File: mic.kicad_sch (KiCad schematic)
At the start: 0 parts

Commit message: added ADAU7002 Symbol
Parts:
- added U3: ~, symbol mic_patch_parts:AUD_00001
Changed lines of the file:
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@@
 	(generator_version "8.0")
 	(paper "A4")
+	(symbol
+		(lib_id "mic_patch_parts:AUD_00001")
+		(at 59.69 43.18 0)
+		(unit 1)
+		(exclude_from_sim no)
+		(in_bom yes)
+		(on_board yes)
+		(dnp no)
+		(fields_autoplaced yes)
+		(property "Reference" "U3"
+			(at 59.69 27.94 0)
+			(effects
+				(font
+					(size 1.27 1.27)
+				)
+			)
+		)
+		(property "Value" "~"
+			(at 59.69 29.21 0)
+			(effects
+				(font
+					(size 1.27 1.27)
+				)
+			)
+		)
+		(property "Footprint" ""
+			(at 66.294 51.308 0)
+			(effects
+				(font
+					(size 1.27 1.27)
+				)
+				(hide yes)
+			)
+		)
+		(property "Datasheet" "https://www.lcsc.com/datasheet/lcsc_datasheet_2001132235_Analog-Devices-ADAU7002ACBZ-R7_C481886.pdf"
+			(at 65.024 59.69 0)
+			(effects
+				(font
+					(size 1.27 1.27)
+				)
+				(hide yes)
+			)
+		)
+		(property "Description" ""
+			(at 62.484 32.004 0)
+			(effects
+				(font
+					(size 1.27 1.27)
+				)
+				(hide yes)
+			)
+		)
+		(property "Desc" "ADAU7002 I2S to PDM Converter"
+			(at 59.69 31.75 0)
+			(effects
+				(font
+					(size 1.27 1.27)
+				)
+			)
+		)
+		(property "LCSC PNs" "C481886"
+			(at 67.31 53.594 0)
+			(effects
+				(font
+					(size 1.27 1.27)
+				)
+				(hide yes)
+			)
+		)
+		(property "MPNs" "ADAU7002ACBZ-R7"
+			(at 59.69 34.29 0)
+			(effects
+				(font
+					(size 1.27 1.27)
+				)
+			)
+		)
+		(pin "B1"
+		)
+		(pin "A1"
+		)
+		(pin "A2"
+		)
+		(pin "B2"
+		)
+		(pin "C1"
+		)
+		(pin "C2"
+		)
+		(pin "D1"
+		)
+		(pin "D2"
+		)
+		(instances
+			(project "mic_patch_v1"
+				(path "/5448a297-4261-40a5-8009-47199bfe22cb/134a282e-9ca3-4100-8ce3-f798951ef007"
+					(reference "U3")
+					(unit 1)
+				)
+			)
+		)
+	)
 )

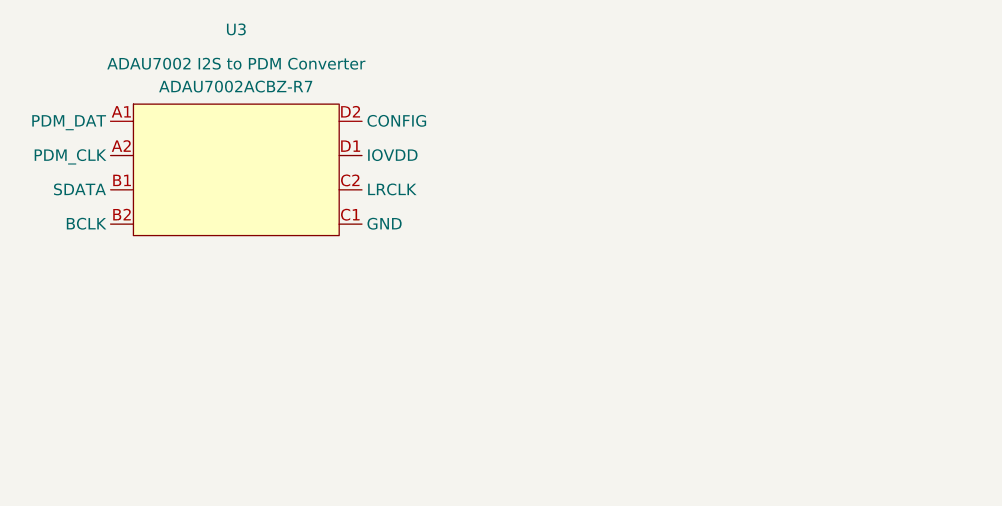
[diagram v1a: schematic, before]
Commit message: added MEMS microphone symbol
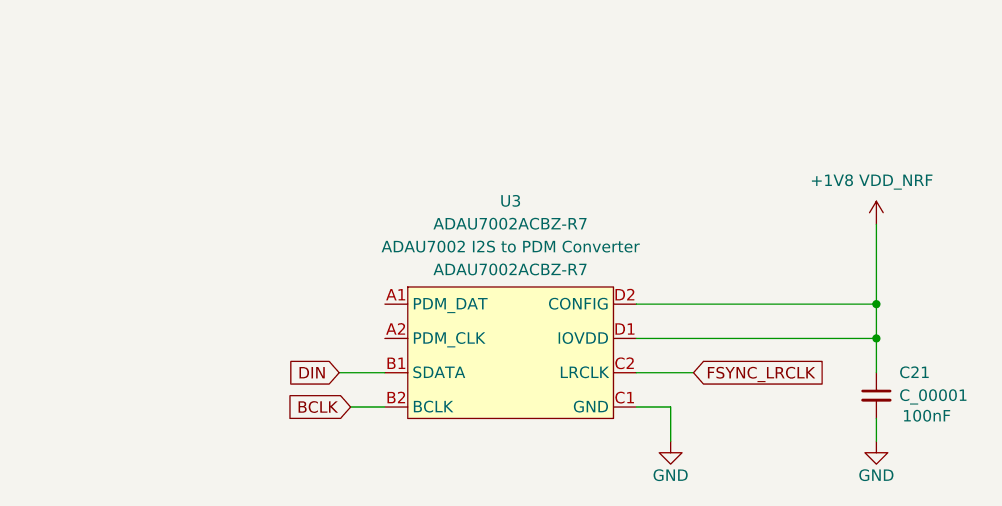
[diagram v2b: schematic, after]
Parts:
- added C21: C_00001, symbol mic_patch_parts:C_00001
- U3: value ~ -> ADAU7002ACBZ-R7
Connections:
- net DIN: now reaches U3.B1 (SDATA)
- net BCLK: now reaches U3.B2 (BCLK)
- net GND: now reaches U3.C1 (GND)
- net GND: now also C21.2
- net FSYNC_LRCLK: now reaches U3.C2 (LRCLK)
- net +1V8 VDD_NRF: now reaches U3.D1 (IOVDD)
- net +1V8 VDD_NRF: now also U3.D2 (CONFIG), C21.1

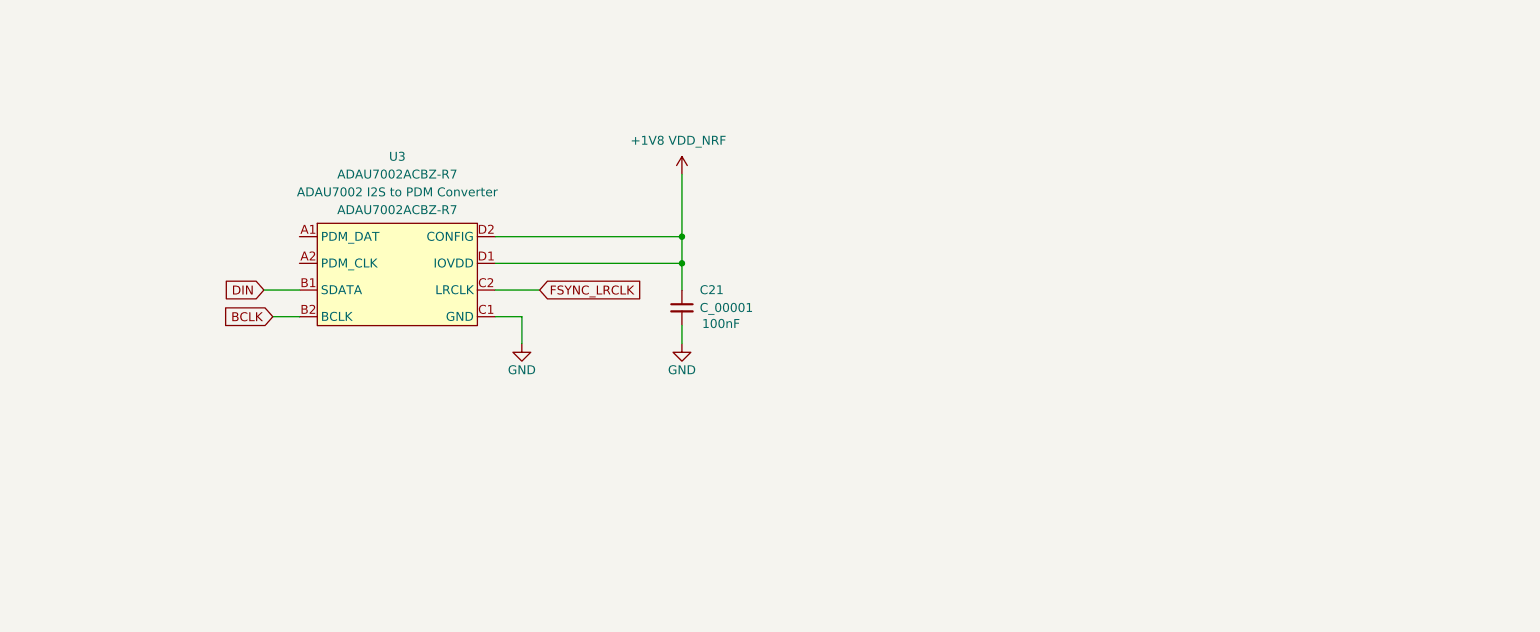
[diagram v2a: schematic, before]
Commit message: added rudimentary RF matching network
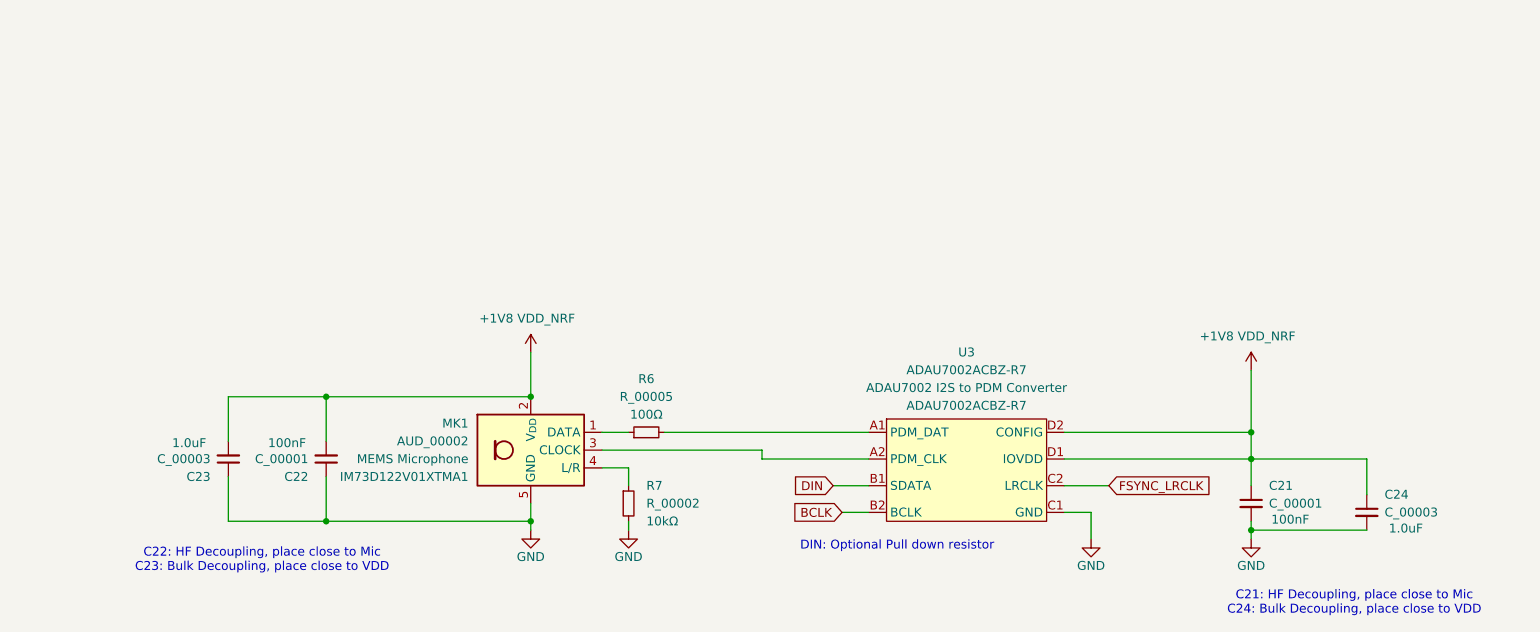
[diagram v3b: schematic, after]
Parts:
- added C22: C_00001, symbol mic_patch_parts:C_00001
- added C23, C24: C_00003, symbol mic_patch_parts:C_00003
- added MK1: AUD_00002, symbol mic_patch_parts:AUD_00002
- added R6: R_00005, symbol mic_patch_parts:R_00005
- added R7: R_00002, symbol mic_patch_parts:R_00003
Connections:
- net +1V8 VDD_NRF: now also C22.2, C23.2, C24.1, MK1.2 (V_{DD})
- net GND: now also C22.1, C23.1, C24.2, MK1.5 (GND), R7.2
- net at U3.A1 (PDM_DAT): now also R6.2
- net at U3.A2 (PDM_CLK): now also MK1.3 (CLOCK)
- new net: MK1.1 (DATA), R6.1
- new net: MK1.4 (L/R), R7.1
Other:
- note added: "C21: HF Decoupling, place close to Mic C24: Bulk Decoupling, place close to VDD"
- note added: "C22: HF Decoupling, place close to Mic C23: Bulk Decoupling, place close to VDD"
- note added: "DIN: Optional Pull down resistor"
- moved on the sheet: C21, U3

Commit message: updated power supply to 3.0V to support micro SD card
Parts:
- removed C24: C_00003, symbol mic_patch_parts:C_00003
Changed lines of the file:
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@@
-	)
-	(junction
-		(at 212.09 100.33)
-		(diameter 0)
-		(color 0 0 0 0)
 	)
 	(junction
@@
 	(wire
 		(pts
-			(xy 212.09 90.17) (xy 228.6 90.17)
-		)
-		(stroke
-			(width 0)
-			(type default)
-		)
-	)
-	(wire
-		(pts
-			(xy 212.09 99.06) (xy 212.09 100.33)
+			(xy 212.09 99.06) (xy 212.09 101.6)
 		)
 		(stroke
@@
 	(wire
 		(pts
-			(xy 212.09 100.33) (xy 228.6 100.33)
-		)
-		(stroke
-			(width 0)
-			(type default)
-		)
-	)
-	(wire
-		(pts
 			(xy 66.04 92.71) (xy 66.04 99.06)
 		)
@@
 		(pts
 			(xy 185.42 90.17) (xy 212.09 90.17)
-		)
-		(stroke
-			(width 0)
-			(type default)
-		)
-	)
-	(wire
-		(pts
-			(xy 212.09 100.33) (xy 212.09 101.6)
-		)
-		(stroke
-			(width 0)
-			(type default)
-		)
-	)
-	(wire
-		(pts
-			(xy 228.6 90.17) (xy 228.6 95.25)
 		)
 		(stroke
@@
 					(unit 1)
 				)
-			)
-		)
-	)
-	(symbol
-		(lib_id "mic_patch_parts:C_00003")
-		(at 228.6 97.79 0)
-		(unit 1)
-		(exclude_from_sim no)
-		(in_bom yes)
-		(on_board yes)
-		(dnp no)
-		(fields_autoplaced yes)
-		(property "Reference" "C24"
-			(at 231.14 95.25 0)
-			(do_not_autoplace yes)
-			(effects
-				(font
-					(size 1.27 1.27)
-				)
-				(justify left)
-			)
-		)
-		(property "Value" "C_00003"
-			(at 231.14 97.79 0)
-			(do_not_autoplace yes)
-			(effects
-				(font
-					(size 1.27 1.27)
-				)
-				(justify left)
-			)
-		)
-		(property "Footprint" ""
-			(at 203.2 99.06 0)
-			(effects
-				(font
-					(size 1.27 1.27)
-				)
-				(hide yes)
-			)
-		)
-		(property "Datasheet" "~"
-			(at 228.6 97.79 0)
-			(effects
-				(font
-					(size 1.27 1.27)
-				)
-				(hide yes)
-			)
-		)
-		(property "Description" "1.0uF"
-			(at 234.188 100.076 0)
-			(do_not_autoplace yes)
-			(effects
-				(font
-					(size 1.27 1.27)
-				)
-			)
-		)
-		(property "Desc" ""
-			(at 231.14 100.33 0)
-			(do_not_autoplace yes)
-			(effects
-				(font
-					(size 1.27 1.27)
-				)
-				(justify left)
-			)
-		)
-		(property "MPNs" ""
-			(at 207.01 90.17 0)
-			(effects
-				(font
-					(size 1.27 1.27)
-				)
-				(hide yes)
-			)
-		)
-		(property "LCSC PNs" ""
-			(at 208.28 95.25 0)
-			(effects
-				(font
-					(size 1.27 1.27)
-				)
-				(hide yes)
-			)
-		)
-		(pin "1"
-		)
-		(pin "2"
-		)
-		(instances
-			(project "mic_patch_v1"
-				(path "/5448a297-4261-40a5-8009-47199bfe22cb/134a282e-9ca3-4100-8ce3-f798951ef007"
-					(reference "C24")
-					(unit 1)
-				)

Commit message: routed pins for SD card
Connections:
- net +1V8 VDD_NRF renamed +3V0 VDD_NRF
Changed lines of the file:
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@@
 			)
 		)
-		(property "Value" "+1V8 VDD_NRF"
+		(property "Value" "+3V0 VDD_NRF"
 			(at 211.582 72.644 0)
 			(effects
@@
 			)
 		)
-		(property "Value" "+1V8 VDD_NRF"
+		(property "Value" "+3V0 VDD_NRF"
 			(at 108.712 70.104 0)
 			(effects

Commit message: added schmatic symbols and footprints for key capacitors, selected LCXO crystal to use internal caps
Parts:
- C21, C22: footprint (none) -> Capacitor_SMD:C_0402_1005Metric; LCSC PNs (none) -> C25744; MPNs (none) -> 0402WGF1002TCE
- MK1: footprint (none) -> mic_patch_parts:AUD_00002; LCSC PNs C5119248 -> C5563886
- R7: footprint (none) -> Resistor_SMD:R_0402_1005Metric; LCSC PNs (none) -> C25744; MPNs (none) -> 0402WGF1002TCE
- U3: footprint (none) -> mic_patch_parts:ADAU7002ACBZ-R7
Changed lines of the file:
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@@
 			)
 		)
-		(property "Footprint" ""
+		(property "Footprint" "mic_patch_parts:ADAU7002ACBZ-R7"
 			(at 178.054 99.568 0)
 			(effects
@@
 			)
 		)
-		(property "Footprint" ""
+		(property "Footprint" "Capacitor_SMD:C_0402_1005Metric"
 			(at 186.69 97.79 0)
 			(effects
@@
 			)
 		)
-		(property "MPNs" ""
+		(property "MPNs" "0402WGF1002TCE"
 			(at 190.5 88.9 0)
 			(effects
@@
 			)
 		)
-		(property "LCSC PNs" ""
+		(property "LCSC PNs" "C25744"
 			(at 191.77 93.98 0)
 			(effects
@@
 			)
 		)
-		(property "Footprint" ""
+		(property "Footprint" "Capacitor_SMD:C_0402_1005Metric"
 			(at 105.41 88.9 0)
 			(effects
@@
 			)
 		)
-		(property "MPNs" ""
+		(property "MPNs" "0402WGF1002TCE"
 			(at 101.6 97.79 0)
 			(effects
@@
 			)
 		)
-		(property "LCSC PNs" ""
+		(property "LCSC PNs" "C25744"
 			(at 100.33 92.71 0)
 			(effects
@@
 			)
 		)
-		(property "Footprint" ""
+		(property "Footprint" "mic_patch_parts:AUD_00002"
 			(at 109.22 69.85 0)
 			(effects
@@
 			)
 		)
-		(property "LCSC PNs" "C5119248"
+		(property "LCSC PNs" "C5563886"
 			(at 86.868 83.058 0)
 			(effects
@@
 			)
 		)
-		(property "Footprint" ""
+		(property "Footprint" "Resistor_SMD:R_0402_1005Metric"
 			(at 123.19 96.52 0)
 			(effects
@@
 			)
 		)
-		(property "Description" "10kΩ resistor"
+		(property "Description" "10kΩ resistor 0402"
 			(at 123.19 96.52 0)
 			(effects
@@
 			)
 		)
-		(property "MPNs" ""
+		(property "MPNs" "0402WGF1002TCE"
 			(at 123.19 96.52 0)
 			(effects
@@
 			)
 		)
-		(property "LCSC PNs" ""
+		(property "LCSC PNs" "C25744"
 			(at 123.19 96.52 0)
 			(effects

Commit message: added all footprints for power module
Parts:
- C23: footprint (none) -> Capacitor_SMD:C_0402_1005Metric; LCSC PNs (none) -> C52923; MPNs (none) -> CL05A105KA5NQNC
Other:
- note added: "MAKE SMALLER"
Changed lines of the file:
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@@
+		)
+	)
+	(text "MAKE SMALLER"
+		(exclude_from_sim no)
+		(at 54.356 82.55 0)
+		(effects
+			(font
+				(size 1.27 1.27)
+			)
 		)
 	)
@@
 			)
 		)
-		(property "Footprint" ""
+		(property "Footprint" "Capacitor_SMD:C_0402_1005Metric"
 			(at 91.44 88.9 0)
 			(effects
@@
 			)
 		)
-		(property "Description" "1.0uF"
+		(property "Description" "1.0uF 0402"
 			(at 60.452 87.884 0)
 			(do_not_autoplace yes)
@@
 			)
 		)
-		(property "MPNs" ""
+		(property "MPNs" "CL05A105KA5NQNC"
 			(at 87.63 97.79 0)
 			(effects
@@
 			)
 		)
-		(property "LCSC PNs" ""
+		(property "LCSC PNs" "C52923"
 			(at 86.36 92.71 0)
 			(effects

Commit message: added footprints for every part
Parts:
- R6: footprint (none) -> Resistor_SMD:R_0402_1005Metric; LCSC PNs (none) -> C25076; MPNs (none) -> 0402WGF1000TCE
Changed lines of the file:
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@@
 			)
 		)
-		(property "Footprint" ""
+		(property "Footprint" "Resistor_SMD:R_0402_1005Metric"
 			(at 125.73 86.36 0)
 			(effects
@@
 			)
 		)
-		(property "MPNs" ""
+		(property "MPNs" "0402WGF1000TCE"
 			(at 125.73 86.36 0)
 			(effects
@@
 			)
 		)
-		(property "LCSC PNs" ""
+		(property "LCSC PNs" "C25076"
 			(at 125.73 86.36 0)
 			(effects
